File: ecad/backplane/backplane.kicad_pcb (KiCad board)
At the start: 2 copper layers, 220 x 160 mm, 25 parts, among them J1 10145891-0320J13LF, J2 10145891-0320J13LF, J3 10145891-0320J13LF, J4 10145891-0320J13LF, J5 USB4105-GF-A, J6 5017868090, U1 MCP16331x-xCH

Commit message: Files for JLCPCB
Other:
- board text added: "rev. 01 3/17/2025"
- board text removed: "rev. 01 3/14/2025"
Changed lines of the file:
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@@
 			(layer "F.Mask"
 				(type "Top Solder Mask")
-				(color "Black")
+				(color "Green")
 				(thickness 0.01)
 			)
@@
 			(layer "B.Mask"
 				(type "Bottom Solder Mask")
-				(color "Black")
+				(color "Green")
 				(thickness 0.01)
 			)
@@
 		)
 	)
-	(gr_text "rev. 01 3/14/2025"
+	(gr_text "rev. 01 3/17/2025"
 		(at 289.6 217.15 0)
 		(layer "B.SilkS")

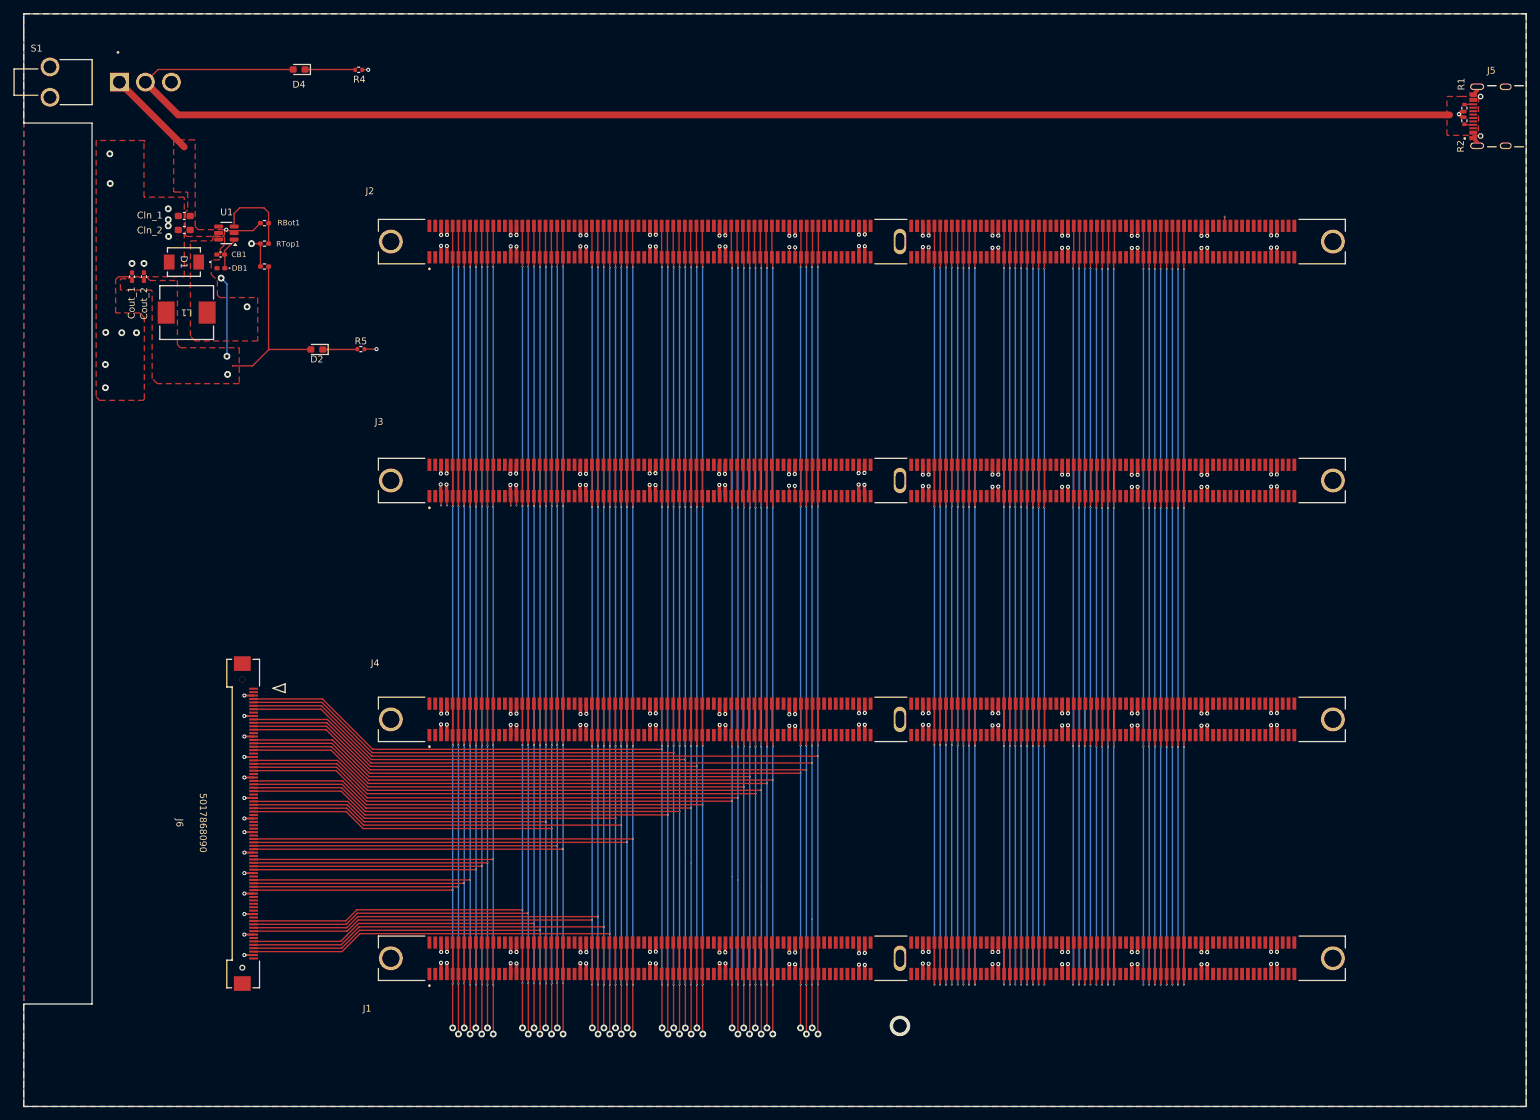
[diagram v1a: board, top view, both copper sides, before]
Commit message: increase via sizes
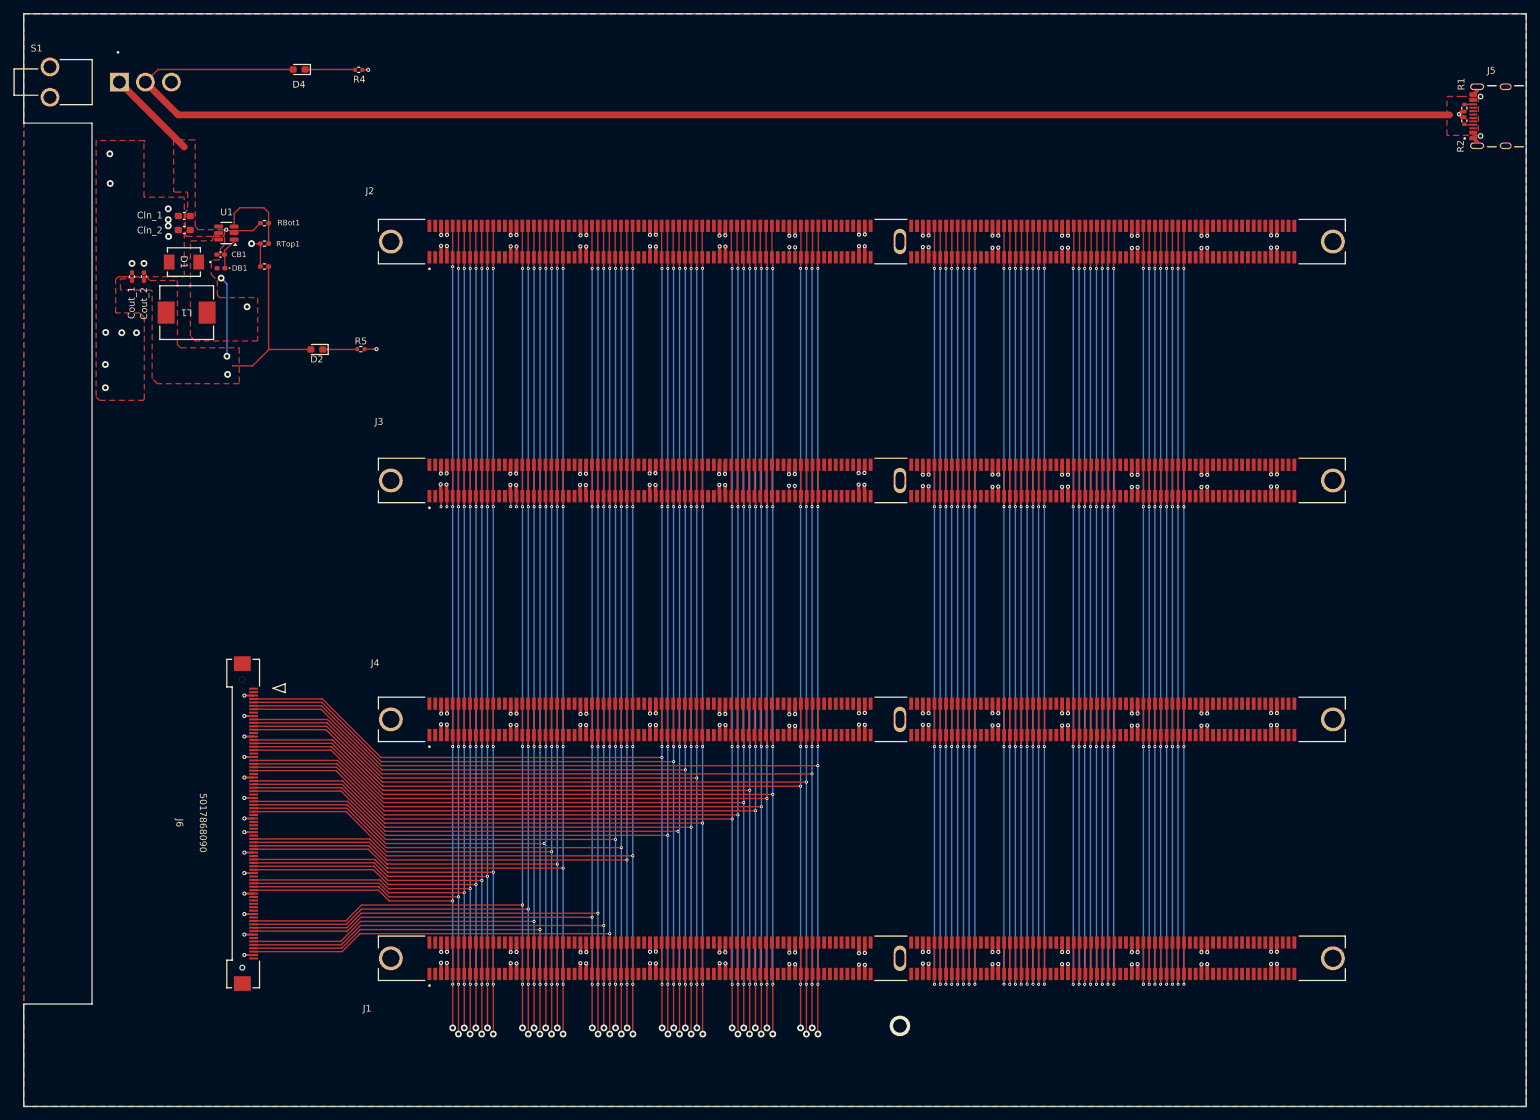
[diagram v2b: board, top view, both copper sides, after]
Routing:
- net D5: track 181.4 -> 182.8 mm
- net A5: track 191.5 -> 192.8 mm
- net unconnected-(J2-Pad276): track 1.35 -> 0.00 mm, vias 1 -> 0
- net A4: track 189.8 -> 191.1 mm
- net D4: track 179.6 -> 180.9 mm
- net PROT: track 198.9 -> 200.1 mm
- net INTE: track 200.6 -> 201.7 mm
- net WAIT: track 202.1 -> 203.3 mm
- net D7: track 182.0 -> 183.2 mm
- net HLDA: track 204.0 -> 205.1 mm
- net D6: track 180.3 -> 181.4 mm
- net A12: track 207.5 -> 208.6 mm
- net A6: track 190.5 -> 191.6 mm
- net OUT: track 210.9 -> 211.9 mm
- net A13: track 209.3 -> 210.3 mm
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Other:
- board text added: "rev. 01 3/18/2025"
- board text removed: "rev. 01 3/17/2025"

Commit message: enlarge holes to 0.3mm
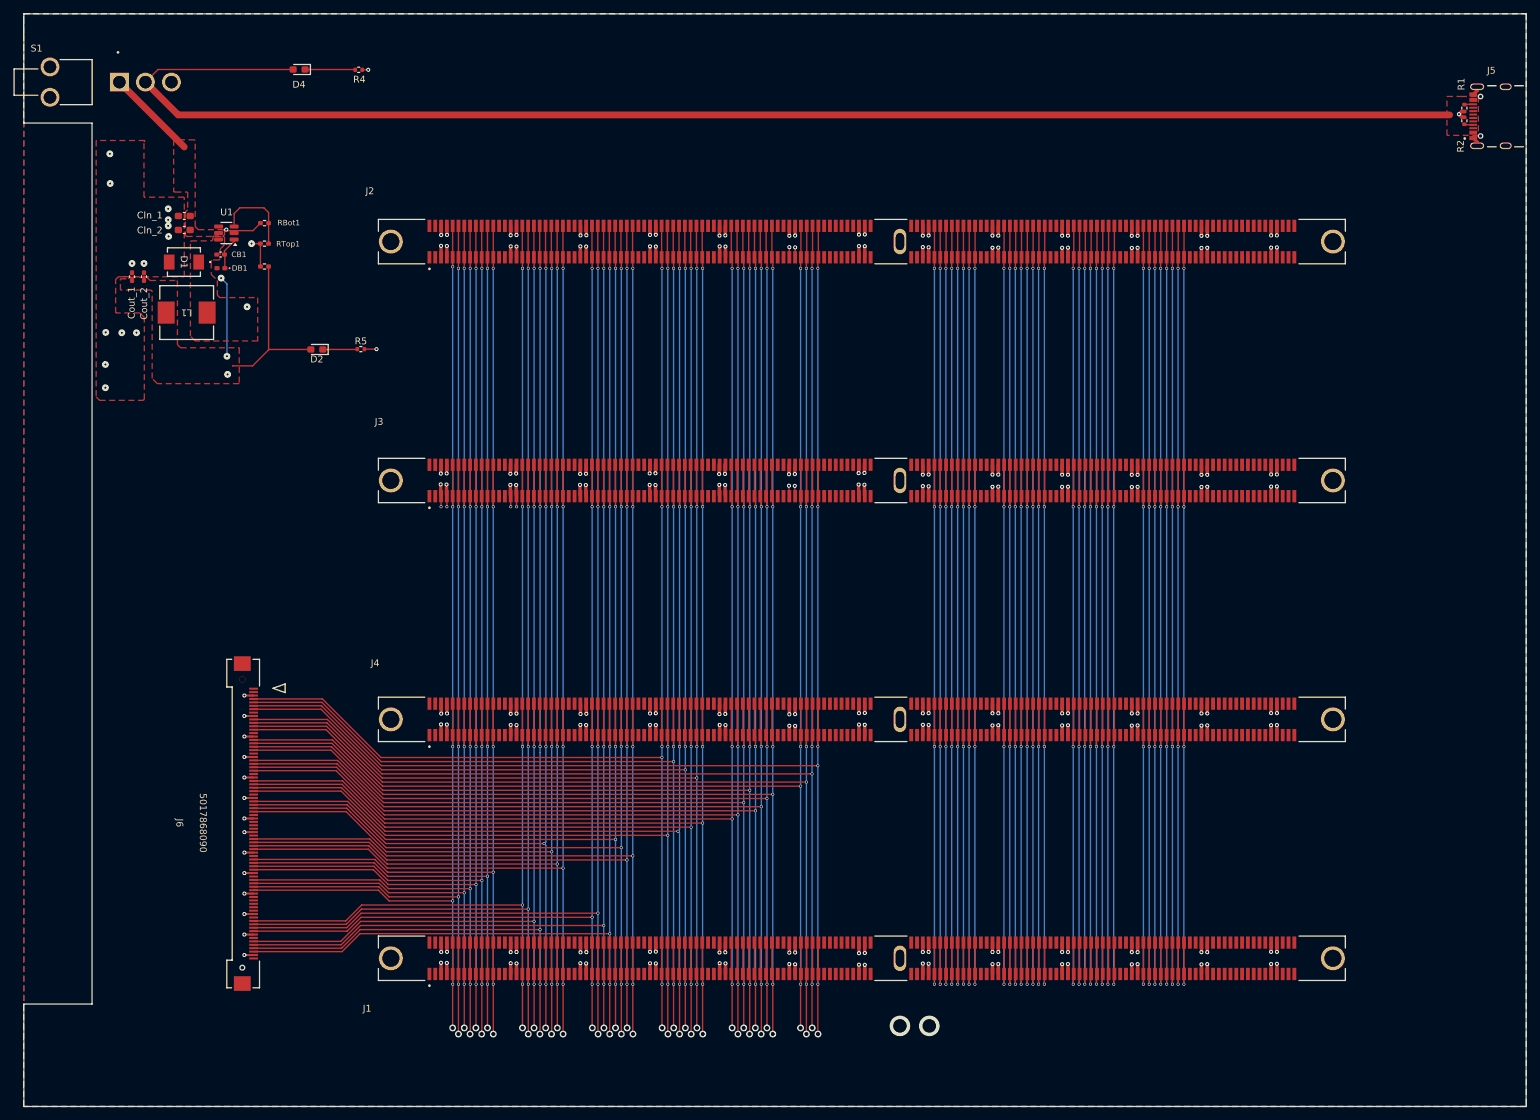
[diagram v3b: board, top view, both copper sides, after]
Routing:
- net GND: vias 243 -> 244
- net 3.3V: vias 3 -> 4
- net (no net): vias 1 -> 0
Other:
- board text added: "rev. 01 3/20/2025"
- board text removed: "rev. 01 3/18/2025"
